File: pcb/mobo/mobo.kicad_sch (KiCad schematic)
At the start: 70 parts, among them J1 ISP, J2 PEEL_MOTOR, J3 DRIVE_MOTOR, J4 SW1, J5 SPRING_FINGERS, J6 SW2, J8 USART1, U1 ATmega328P-A, U2 ATmega328P-M, U4 AP1117-50, U5 MC34063AD, U6 SP308xE, U7 DRV8837, U8 DRV8837, Y1 16MHz

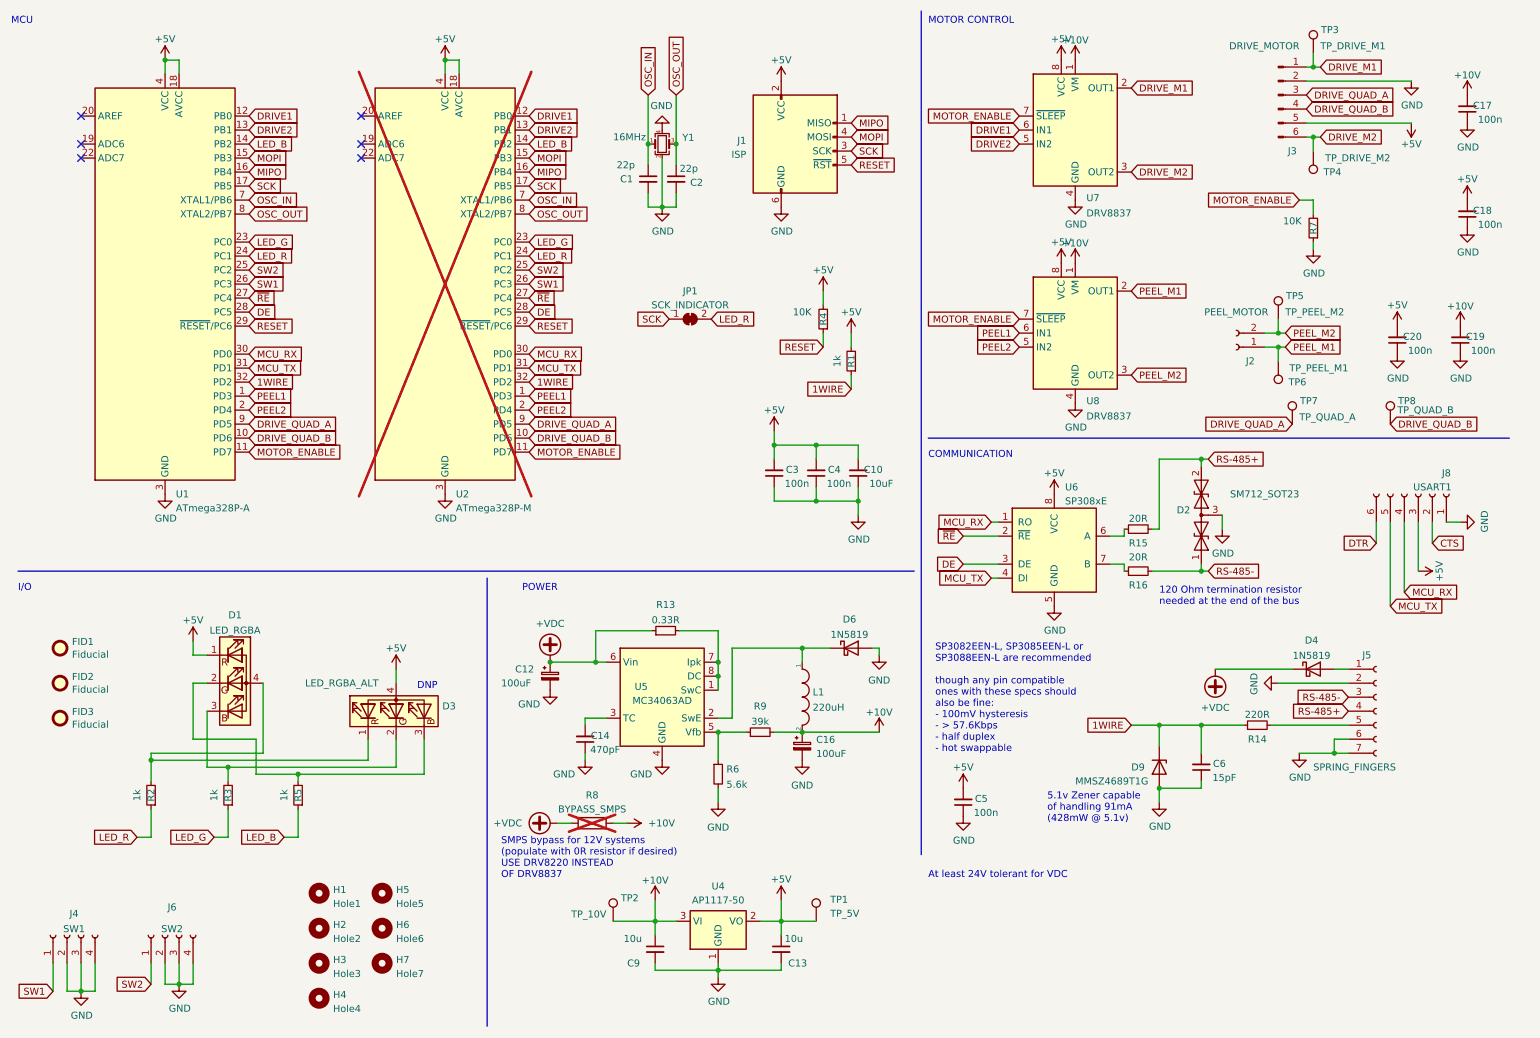
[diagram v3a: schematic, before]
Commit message: Replace ATmega328P with ATmega328PB and improve RS-485 routing
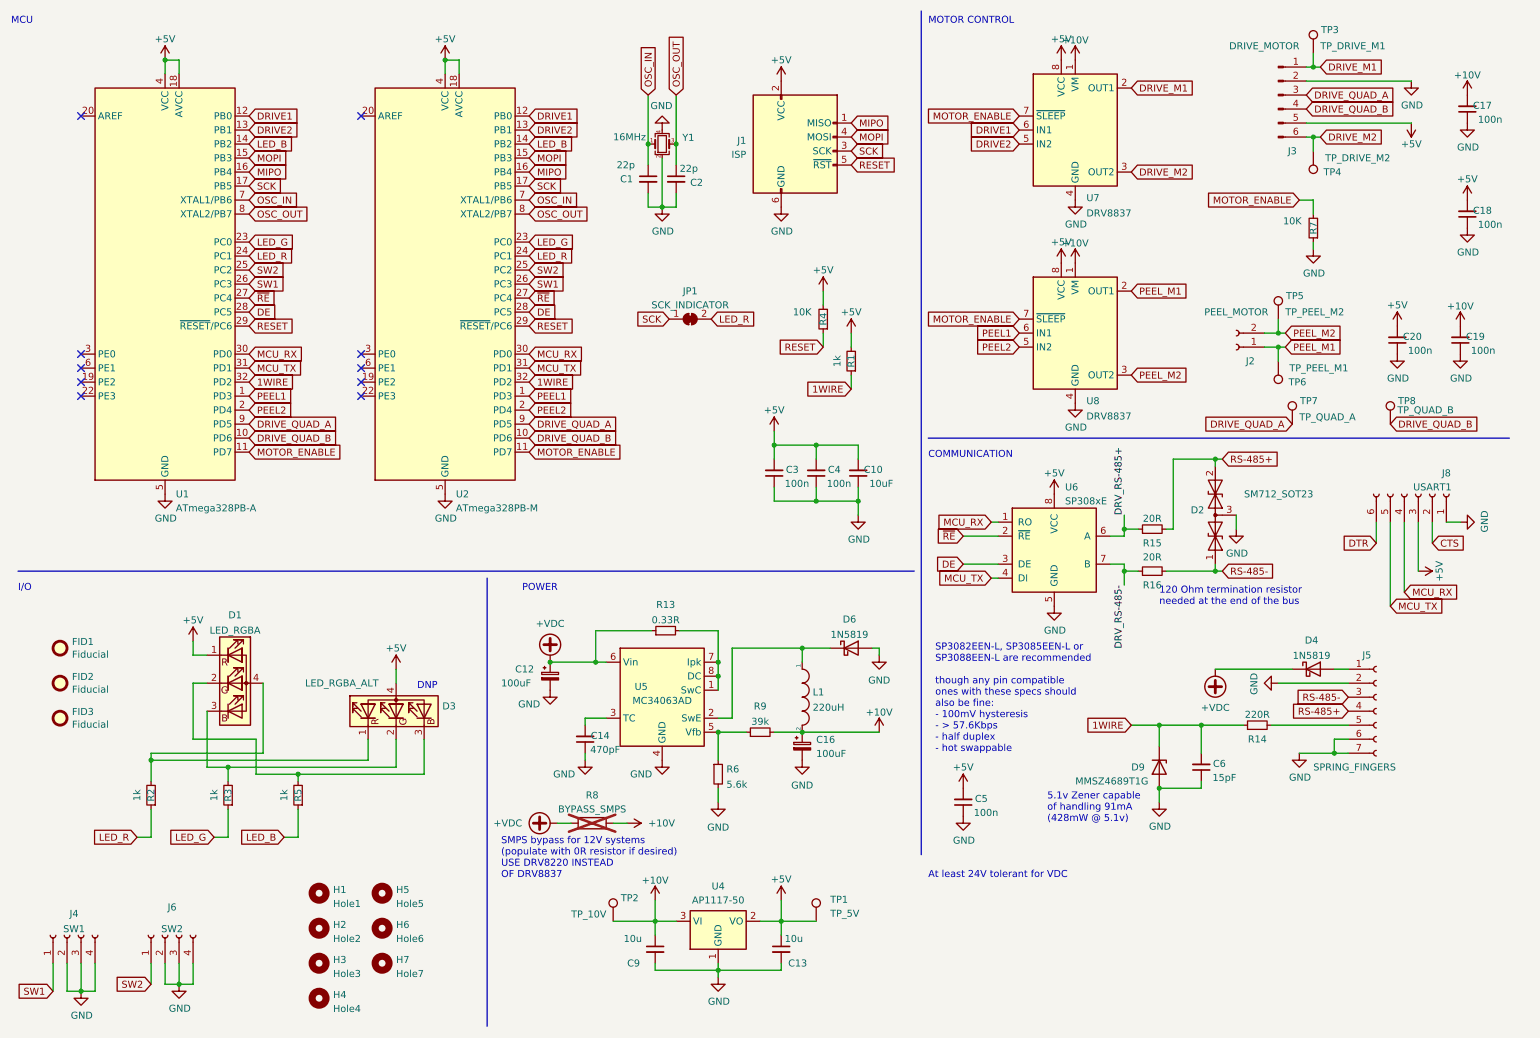
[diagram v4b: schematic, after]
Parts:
- removed U1: ATmega328P-A, Package_QFP:TQFP-32_7x7mm_P0.8mm, symbol MCU_Microchip_ATmega:ATmega328P-A
- removed U2: ATmega328P-M, Package_DFN_QFN:QFN-32-1EP_5x5mm_P0.5mm_EP3.1x3.1mm, symbol MCU_Microchip_ATmega:ATmega328P-M
- added U1: ATmega328PB-A, Package_QFP:TQFP-32_7x7mm_P0.8mm, symbol MCU_Microchip_ATmega:ATmega328PB-A
- added U2: ATmega328PB-M, Package_DFN_QFN:QFN-32-1EP_5x5mm_P0.5mm_EP3.1x3.1mm, symbol MCU_Microchip_ATmega:ATmega328PB-M
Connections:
- net +5V: now also U1.18 (AVCC), U1.4 (VCC), U2.18 (AVCC), U2.4 (VCC)
- net 1WIRE: now also U1.32 (PD2), U2.32 (PD2)
- net DE: now also U1.28 (PC5), U2.28 (PC5)
- net DRIVE1: now also U1.12 (PB0), U2.12 (PB0)
- net DRIVE2: now also U1.13 (PB1), U2.13 (PB1)
- net DRIVE_QUAD_A: now also U1.9 (PD5), U2.9 (PD5)
- net DRIVE_QUAD_B: now also U1.10 (PD6), U2.10 (PD6)
- net GND: now also U1.21 (GND), U1.5 (GND), U2.21 (GND), U2.33 (GND), U2.5 (GND)
- net LED_B: now also U1.14 (PB2), U2.14 (PB2)
- net LED_G: now also U1.23 (PC0), U2.23 (PC0)
- net LED_R: now also U1.24 (PC1), U2.24 (PC1)
- net MCU_RX: now also U1.30 (PD0), U2.30 (PD0)
- net MCU_TX: now also U1.31 (PD1), U2.31 (PD1)
- net MIPO: now also U1.16 (PB4), U2.16 (PB4)
- net MOPI: now also U1.15 (PB3), U2.15 (PB3)
- net MOTOR_ENABLE: now also U1.11 (PD7), U2.11 (PD7)
- net OSC_IN: now also U1.7 (XTAL1/PB6), U2.7 (XTAL1/PB6)
- net OSC_OUT: now also U1.8 (XTAL2/PB7), U2.8 (XTAL2/PB7)
- net PEEL1: now also U1.1 (PD3), U2.1 (PD3)
- net PEEL2: now also U1.2 (PD4), U2.2 (PD4)
- net RESET: now also U1.29 (~{RESET}/PC6), U2.29 (~{RESET}/PC6)
- net SCK: now also U1.17 (PB5), U2.17 (PB5)
- net SW1: now also U1.26 (PC3), U2.26 (PC3)
- net SW2: now also U1.25 (PC2), U2.25 (PC2)
- net ~{RE}: now also U1.27 (PC4), U2.27 (PC4)
- net DRV_RS-485+: now reaches R15.1, U6.6 (A)
- net DRV_RS-485-: now reaches R16.1, U6.7 (B)
- no-connect marks 6 -> 10
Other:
- moved on the sheet: D2, R15, R16

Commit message: Remove vias from pads, Remove paste layer from alt QFN footprint (#14)
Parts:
- U2: footprint Package_DFN_QFN:QFN-32-1EP_5x5mm_P0.5mm_EP3.1x3.1mm -> feeder:QFN-32-1EP_5x5mm_P0.5mm_EP3.1x3.1mm_DNP
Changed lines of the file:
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@@
       (effects (font (size 1.27 1.27)) (justify left))
     )
-    (property "Footprint" "Package_DFN_QFN:QFN-32-1EP_5x5mm_P0.5mm_EP3.1x3.1mm" (at 91.44 62.23 0)
+    (property "Footprint" "feeder:QFN-32-1EP_5x5mm_P0.5mm_EP3.1x3.1mm_DNP" (at 91.44 62.23 0)
       (effects (font (size 1.27 1.27) italic) hide)
     )

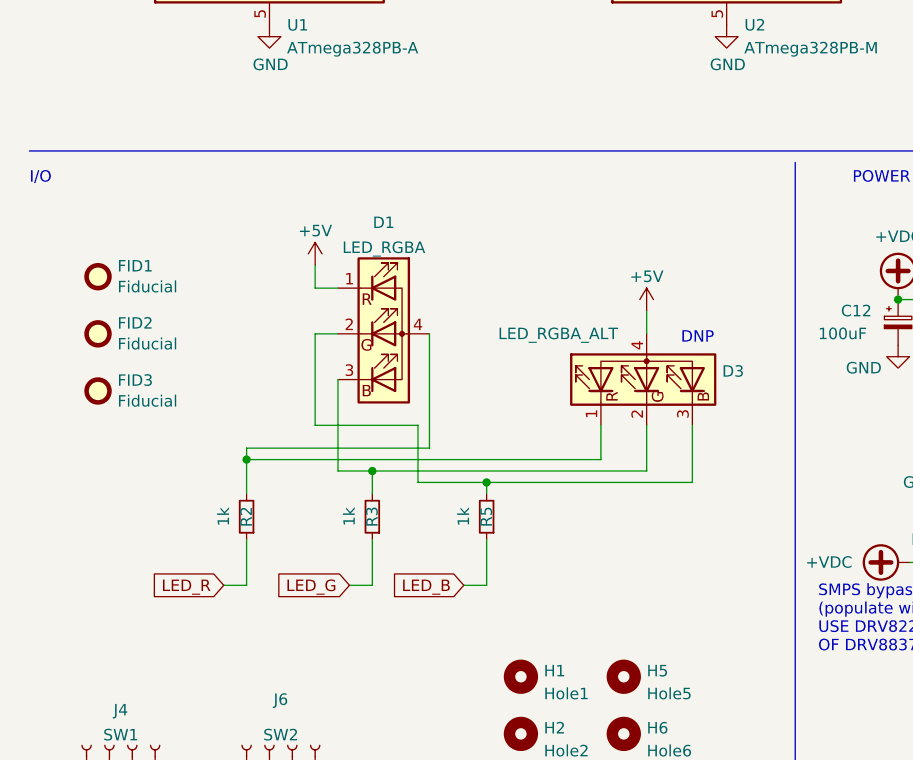
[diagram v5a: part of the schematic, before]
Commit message: Mark LED_RGBA_ALT as DNP, Add MHS110FRGBCT symbol, footprint (#9)
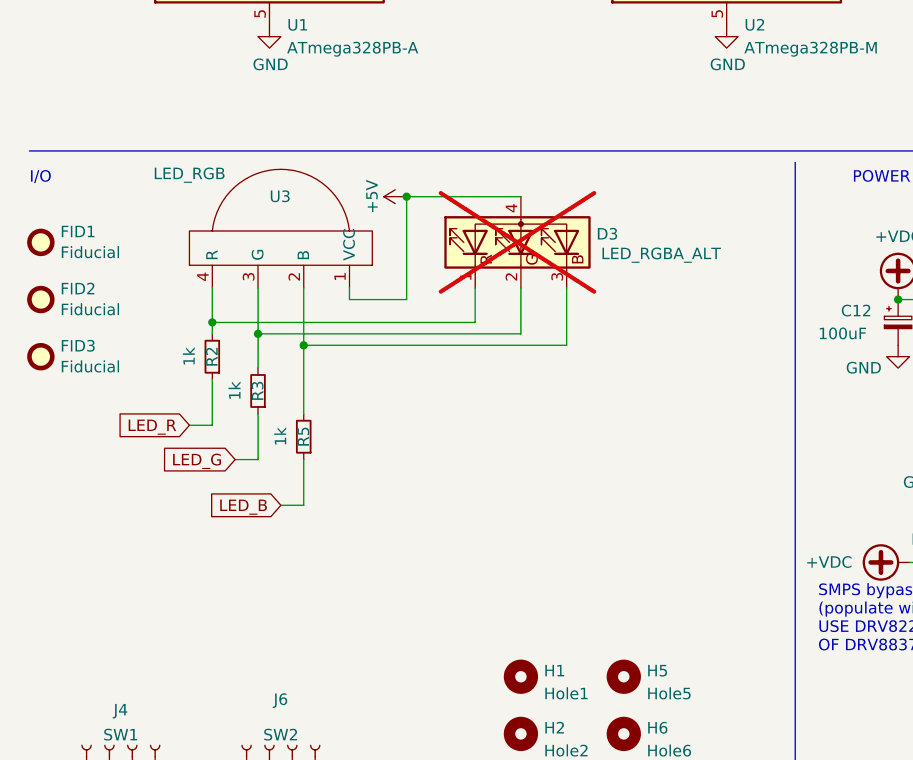
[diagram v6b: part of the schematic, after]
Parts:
- removed D1: LED_RGBA, index:MHS110FRGBCT, symbol Device:LED_RGBA
- added U3: LED_RGB, feeder:MHS110FRGBCT, symbol feeder:MHS110FRGBCT
- D3: now not fitted
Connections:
- net +5V: now also U3.1 (VCC)
- net at D3.2 (GK), R3.2: now also U3.3 (G)
- net at D3.1 (RK), R2.2: now also U3.4 (R)
- net at D3.3 (BK), R5.2: now also U3.2 (B)
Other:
- note removed: "DNP"
- moved on the sheet: FID1, FID2, FID3, R2, R3, R5

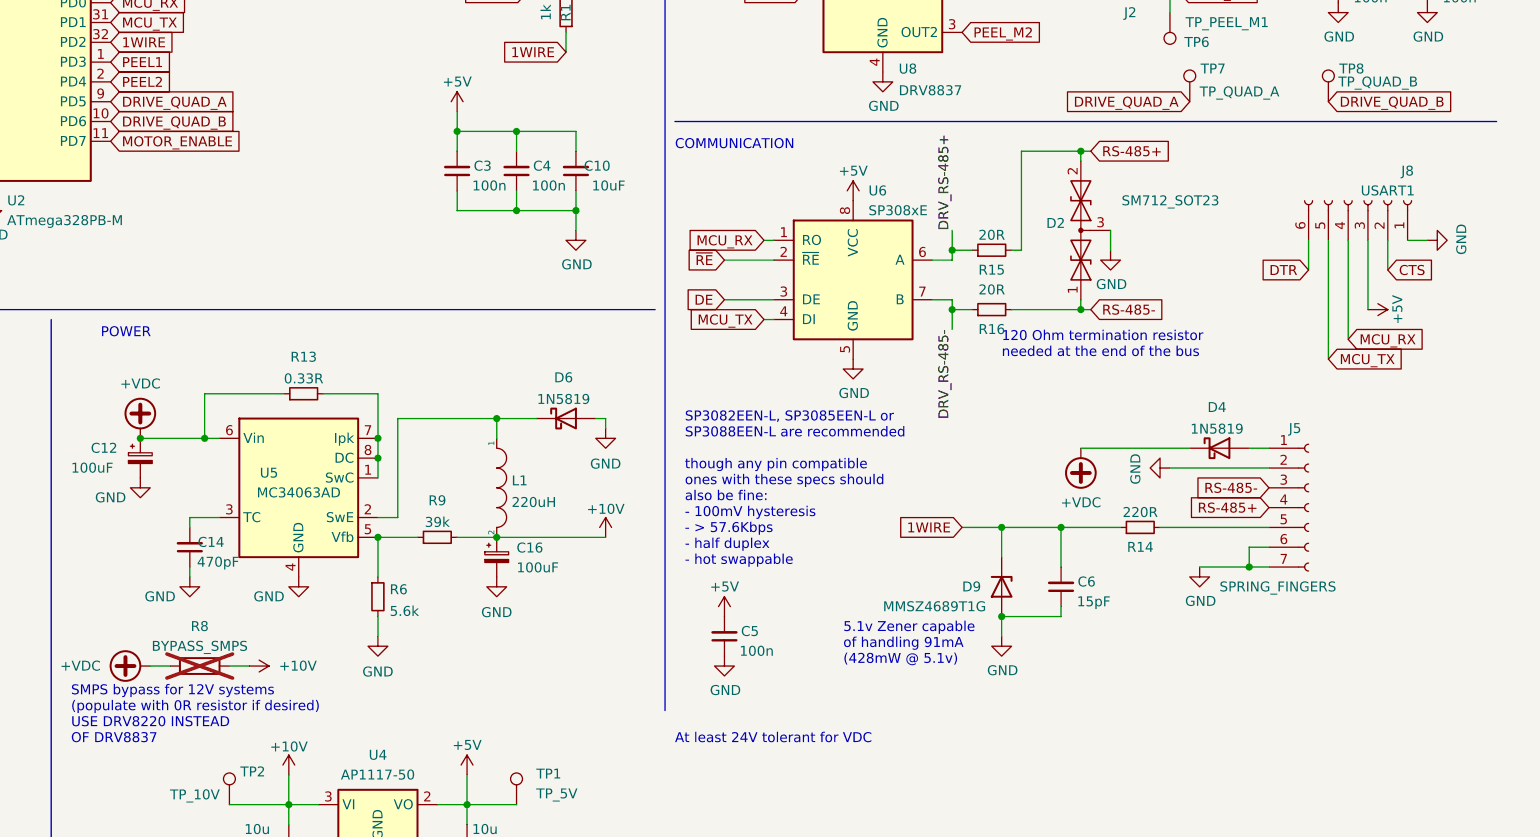
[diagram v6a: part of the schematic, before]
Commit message: Add X and Y caps to RS485 lines (#19), Update symbols
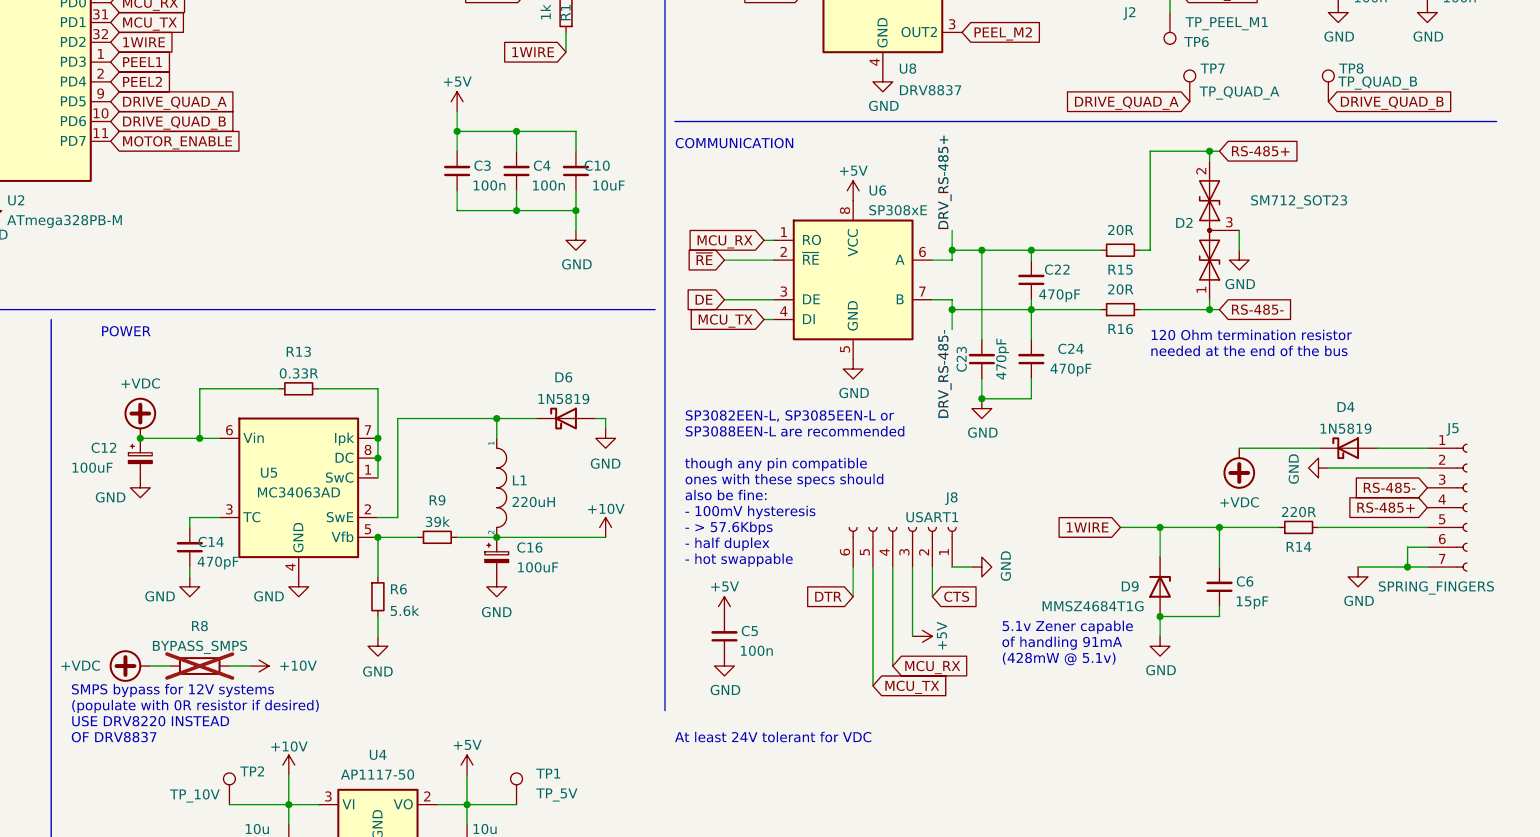
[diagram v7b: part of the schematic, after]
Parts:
- added C22, C23, C24: 470pF, Capacitor_SMD:C_0805_2012Metric, symbol Device:C_Small
- D9: value MMSZ4689T1G -> MMSZ4684T1G
- J2: symbol Connector:Conn_01x02_Female -> Connector:Conn_01x02_Socket
- J3: symbol Connector:Conn_01x06_Male -> Connector:Conn_01x06_Pin
- J4, J6: symbol Connector:Conn_01x04_Female -> Connector:Conn_01x04_Socket
- J5: symbol Connector:Conn_01x07_Female -> Connector:Conn_01x07_Socket
- J8: symbol Connector:Conn_01x06_Female -> Connector:Conn_01x06_Socket
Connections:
- net DRV_RS-485+: now also C22.2, C23.2
- net DRV_RS-485-: now also C22.1, C24.2
- net GND: now also C23.1, C24.1
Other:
- moved on the sheet: C6, D2, D4, D9, J5, J8, R13, R14, R15, R16

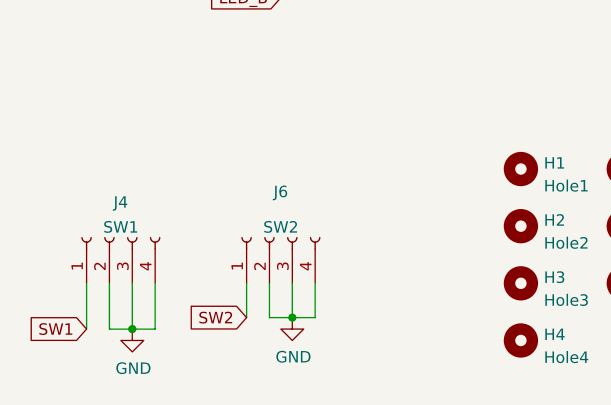
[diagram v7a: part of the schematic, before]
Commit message: Add push button symbol, Update footprints, Cleanup tracks
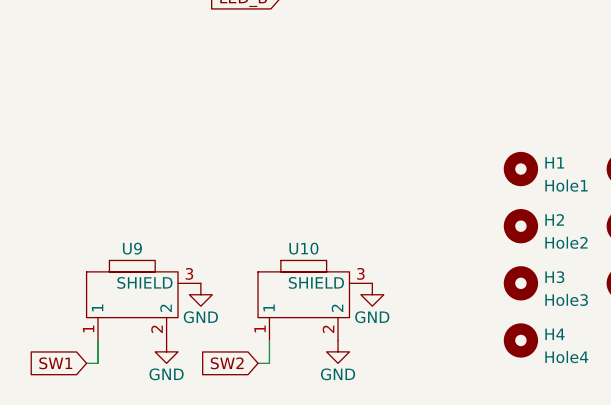
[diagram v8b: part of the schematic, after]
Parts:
- removed J4: SW1, feeder:1TS003B-1400-3500A-CT, symbol Connector:Conn_01x04_Socket
- removed J6: SW2, feeder:1TS003B-1400-3500A-CT, symbol Connector:Conn_01x04_Socket
- added U10, U9: ~, feeder:1TS003B-1400-3500A-CT, symbol feeder:1TS003B-1400-3500A-CT
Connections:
- net GND: now also U10.2, U10.3 (SHIELD), U9.2, U9.3 (SHIELD)
- net SW1: now also U9.1
- net SW2: now also U10.1
